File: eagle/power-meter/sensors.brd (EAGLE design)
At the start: 100 x 74.9 mm, 36 parts

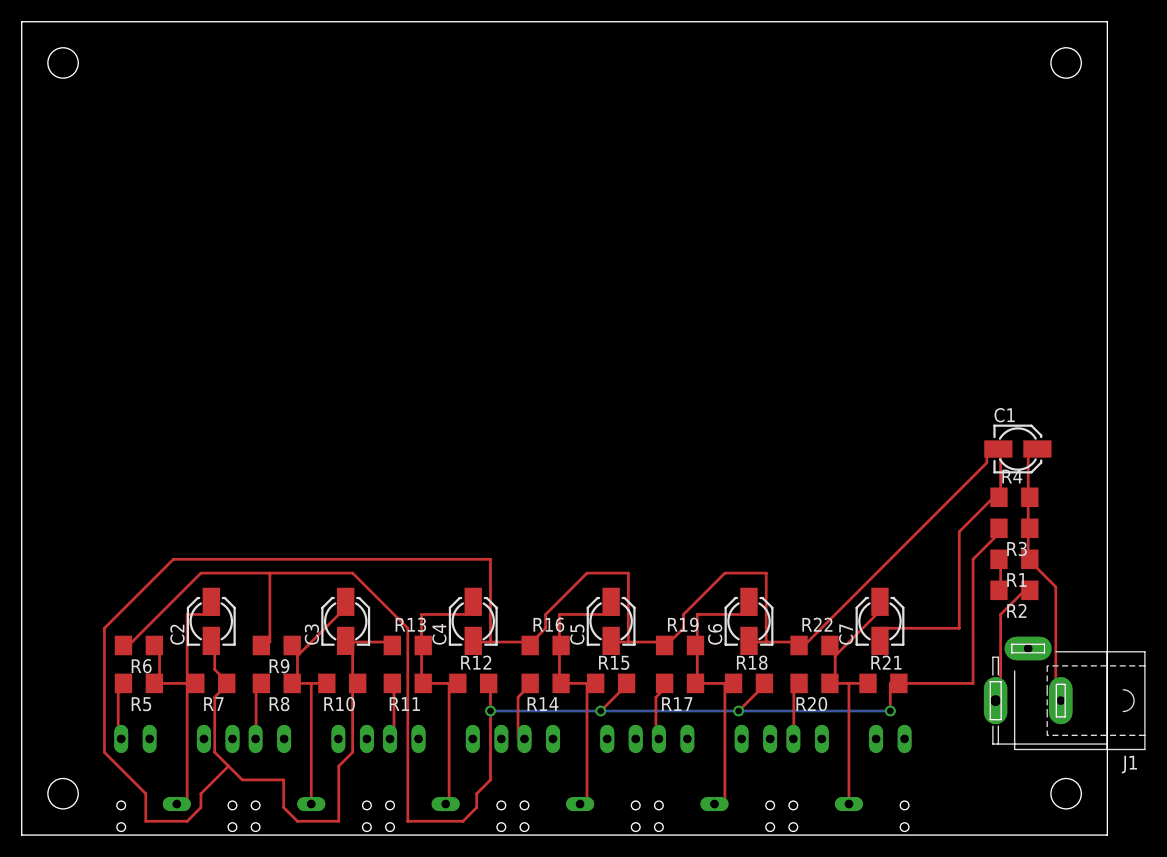
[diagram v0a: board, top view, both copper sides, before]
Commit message: Common Eagle library created. Working on power-node schematics
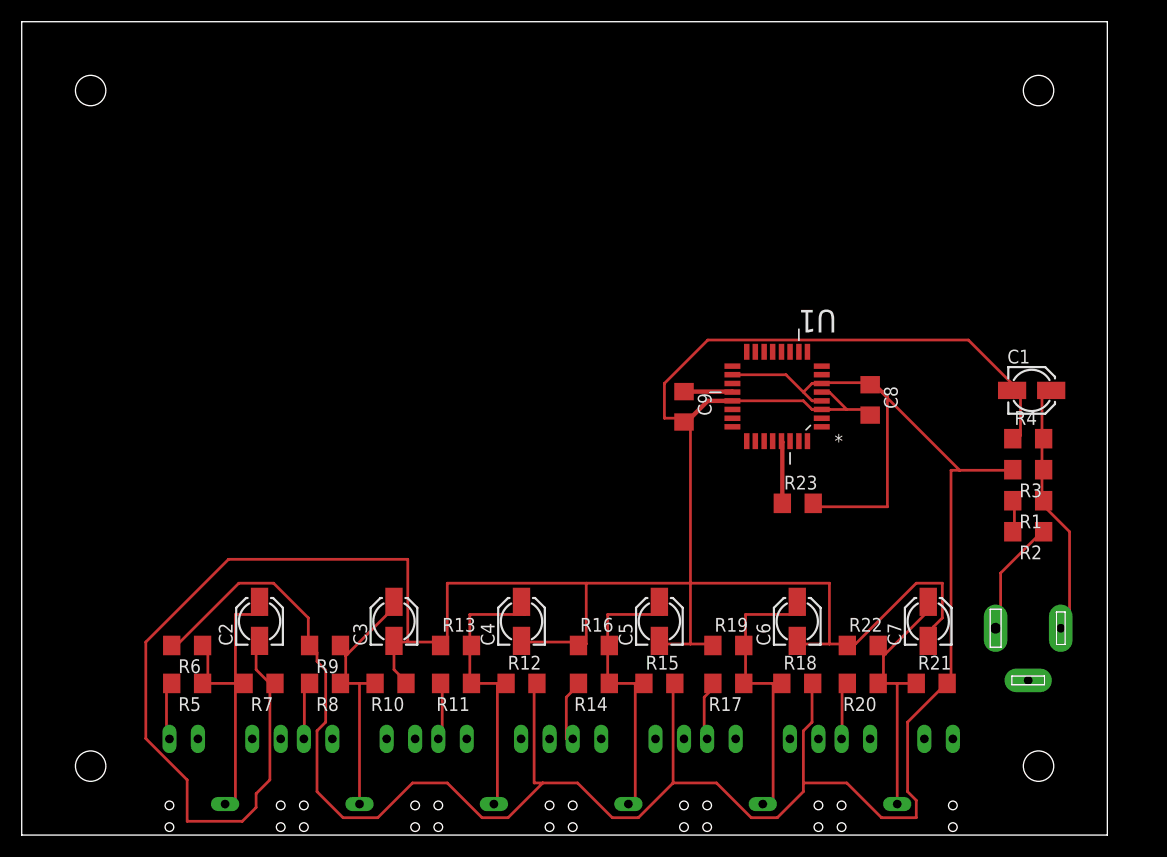
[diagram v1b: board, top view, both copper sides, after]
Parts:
- added C8, C9: 100nF, rcl:C1206
- added R23: 10k, rcl:R1206
- added U1: ATMEGA168A-AU, Atmel_By_element14_Batch_1:QFP80P900X900X120-32N
- JC1: device Jack3.5:15428/BT -> EnergyMonitoring:15428/BT
- moved J1 6.67 mm to (92.7, 19.1), flipped to the bottom, turned to 0 degrees
- moved C1 5.54 mm to (93.0, 41.0)
- moved R4 5.54 mm to (92.7, 36.5)
- moved R1 5.54 mm to (92.7, 30.8)
- moved R2 5.54 mm to (92.7, 27.9)
- moved R3 5.54 mm to (92.7, 33.7)
- moved R17 4.45 mm to (65.1, 14.0)
- moved R19 4.45 mm to (65.1, 17.5)
- moved JC1 4.45 mm to (18.7, 2.86)
- moved C2 4.45 mm to (21.9, 19.7)
- moved C3 4.45 mm to (34.3, 19.7)
- moved C4 4.45 mm to (46.0, 19.7)
- moved C5 4.45 mm to (58.7, 19.7)
- moved JC3 4.45 mm to (43.5, 2.86)
- moved JC4 4.45 mm to (55.9, 2.86)
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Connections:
- new net N$10: R23.1, U1.29
- new net N$11: U1.23
- new net N$12: U1.24
- new net N$13: U1.25
- new net N$14: U1.26
- new net N$15: U1.27
- new net N$16: U1.28
- new net N$9: C9.1, U1.20
- net GND: now also C8.2, C9.2, U1.21, U1.3, U1.5
- net VCC: now also C8.1, R23.2, U1.18, U1.4, U1.6
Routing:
- net VCC: track 144.8 -> 215.1 mm, vias 4 -> 0
- net GND: track 233.2 -> 261.0 mm
- net N$10: track 0.00 -> 5.76 mm
- net N$9: track 0.00 -> 4.50 mm
- net N$1: track 12.1 -> 11.1 mm

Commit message: Working on power-monitor PCB
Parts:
- added U$1: EVQQ2, EnergyMonitoring:EVQQ2
- moved C9 11.5 mm to (67.1, 49.2), turned to 90 degrees
- moved C8 9.47 mm to (83.0, 48.2), turned to 90 degrees
- moved R23 9.28 mm to (78.0, 37.2)
- moved U1 7.95 mm to (74.8, 46.4)
- moved R18 7.41 mm to (65.1, 17.8), turned to 180 degrees
- moved R21 7.41 mm to (77.5, 17.8), turned to 180 degrees
- moved R12 7.13 mm to (40.0, 17.8), turned to 180 degrees
- moved R15 7.13 mm to (52.7, 17.8), turned to 180 degrees
- moved R16 6.70 mm to (58.4, 14.0), turned to 180 degrees
- moved R22 6.70 mm to (83.2, 14.0), turned to 180 degrees
- moved R13 6.70 mm to (45.7, 14.0), turned to 180 degrees
- moved R19 6.70 mm to (70.8, 14.0), turned to 180 degrees
- moved R7 0.95 mm to (21.0, 14.0)
- moved R6 0.32 mm to (15.2, 17.8)
- moved R9 0.32 mm to (27.9, 17.8)
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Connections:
- net N$9 renamed AREF
- removed net N$12: U1.24
- removed net N$13: U1.25
- removed net N$14: U1.26
- removed net N$15: U1.27
- removed net N$16: U1.28
- new net RESET: R23.1, U$1.1, U$1.2, U1.29
- net CT1: now also U1.22
- net CT2: now also U1.23
- net CT3: now also U1.24
- net CT4: now also U1.25
- net CT5: now also U1.26
- net CT6: now also U1.27
- net GND: now also U$1.3, U$1.4
- net N$10: now also U1.7; no longer R23.1, U1.29
- net N$11: now also U1.8; no longer U1.23
- net VT: now also U1.28
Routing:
- net CT1: track 5.84 -> 88.6 mm
- net VCC: track 215.1 -> 138.1 mm, vias 0 -> 7
- net CT2: track 5.62 -> 74.4 mm
- net GND: track 261.0 -> 327.7 mm
- net CT3: track 5.60 -> 61.6 mm
- net CT4: track 6.35 -> 50.1 mm
- net CT5: track 6.35 -> 40.0 mm
- net CT6: track 5.62 -> 34.7 mm
- net VT: track 3.04 -> 30.9 mm
- net RESET: track 0.00 -> 17.6 mm
- net N$10: track 5.76 -> 0.00 mm
- net N$3: track 31.2 -> 25.6 mm
- net N$5: track 28.7 -> 24.0 mm
- net N$7: track 29.4 -> 25.5 mm
- net N$6: track 28.9 -> 25.2 mm
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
